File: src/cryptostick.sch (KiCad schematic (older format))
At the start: 32 parts, among them J1 SIM_JACKET, J2 USB_A, P1 CONN_4, U1 STM32F103TB, U2 CAT6217-330, U3 DF5A5.6JE, X1 12MHz, p1 debug-pin, p2 debug-pin, p3 debug-pin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

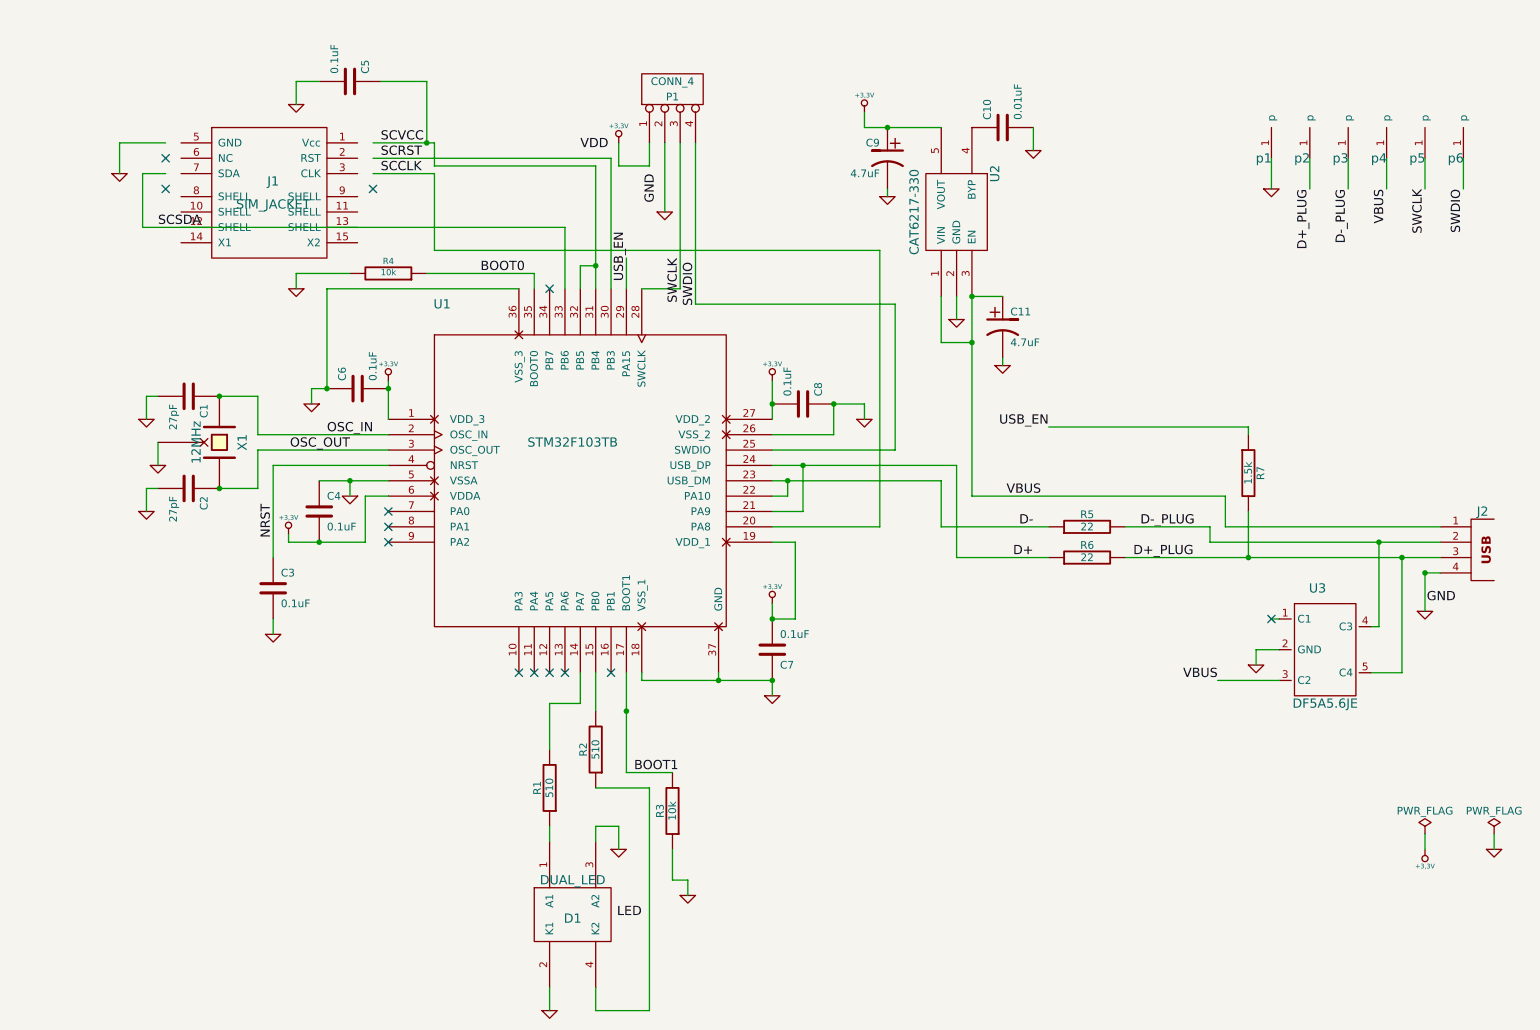
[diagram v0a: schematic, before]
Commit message: V3: - ATECC508 crypto engine - Touch button, SIM jacket used as a touch pad, MTCH101 touch controller (same as used with Nitrokey U2F FIDO stick)
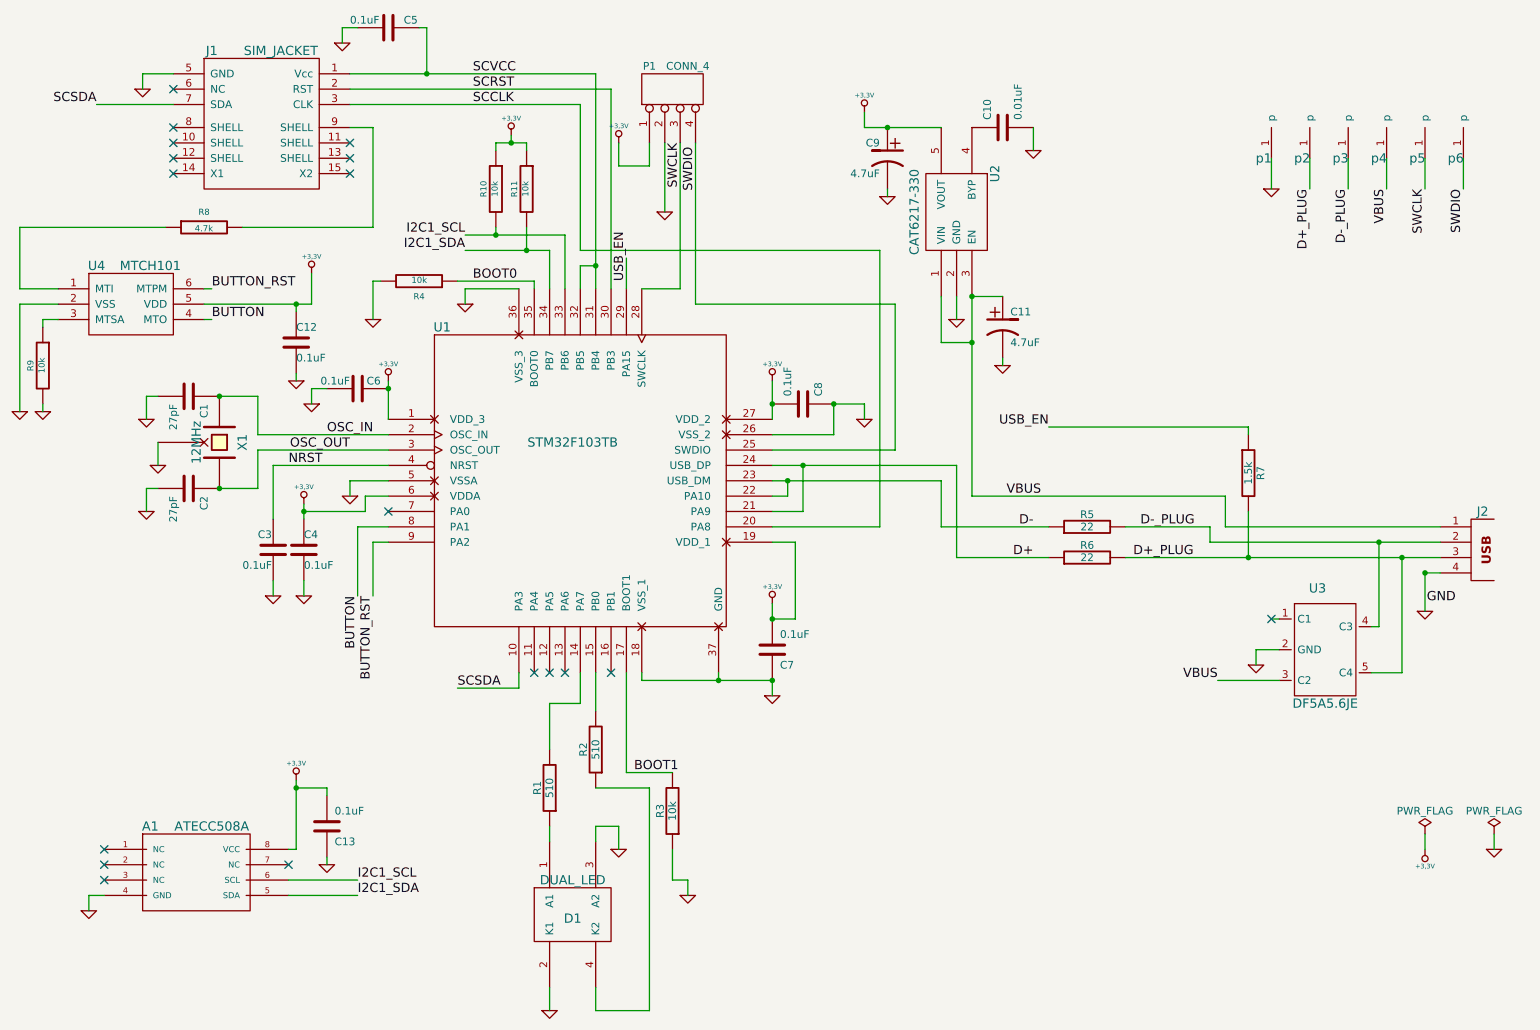
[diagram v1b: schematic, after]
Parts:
- added A1: ATECC508A, Housings_DFN_QFN:DFN-8-1EP_3x3mm_Pitch0.5mm, symbol ATECC508A
- added C12: 0.1uF, C_0402, symbol C-RESCUE-cryptostick
- added C13: 0.1uF, Capacitors_SMD:C_0402, symbol C-RESCUE-cryptostick
- added R10, R11, R9: 10k, r_0402, symbol R-RESCUE-cryptostick
- added R8: 4.7k, r_0402, symbol R-RESCUE-cryptostick
- added U4: MTCH101, symbol MTCH101
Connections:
- net labels added: BUTTON, BUTTON_RST, I2C1_SCL, I2C1_SDA
- net labels removed: LED, VDD
- wire segments 143 -> 181
- no-connect marks 13 -> 18
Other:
- moved on the sheet: C3, C4, C5, J1, R4
